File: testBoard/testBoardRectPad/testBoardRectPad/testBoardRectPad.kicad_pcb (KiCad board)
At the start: 2 copper layers, 1 part

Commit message: intermediate commit
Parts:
- removed the REF** at (105.4, 80.0)
- added REF**: DIP-14_W7.62mm, Package_DIP:DIP-14_W7.62mm, F.Cu at (110.1, 70.0)
- added REF**: SOIC-14_3.9x8.7mm_P1.27mm, Package_SO:SOIC-14_3.9x8.7mm_P1.27mm, F.Cu at (0.00, 0.00)
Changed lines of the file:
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@@
     (tracks 0)
     (zones 0)
-    (modules 1)
+    (modules 2)
     (nets 1)
   )
@@
     (mod_text_size 1 1)
     (mod_text_width 0.15)
-    (pad_size 5.3 7)
-    (pad_drill 0.8001)
+    (pad_size 1.95 0.6)
+    (pad_drill 0)
     (pad_to_mask_clearance 0.051)
     (solder_mask_min_width 0.25)
@@
     (visible_elements FFFFFF7F)
     (pcbplotparams
-      (layerselection 0x00000_ffffffff)
+      (layerselection 0x00000_7fffffff)
       (usegerberextensions false)
       (usegerberattributes false)
@@
       (psnegative false)
       (psa4output false)
-      (plotreference true)
-      (plotvalue true)
+      (plotreference false)
+      (plotvalue false)
       (plotinvisibletext false)
       (padsonsilk false)
@@
     (uvia_drill 0.1)
   )
-  (module Connector_Wire:SolderWirePad_1x01_Drill0.8mm (layer F.Cu)
-    (at 105.41 80.01)
-    (descr "Wire solder connection")
-    (tags connector)
-    (attr virtual)
-    (fp_text reference REF** (at 0 -2.54) (layer F.SilkS)
+  (module Package_DIP:DIP-14_W7.62mm (layer F.Cu)
+    (at 110.1 70)
+    (descr "14-lead though-hole mounted DIP package, row spacing 7.62 mm (300 mils)")
+    (tags "THT DIP DIL PDIP 2.54mm 7.62mm 300mil")
+    (fp_text reference REF** (at 3.81 -2.33) (layer F.SilkS)
       (effects (font (size 1 1) (thickness 0.15)))
     )
-    (fp_text value SolderWirePad_1x01_Drill0.8mm (at 0 2.54) (layer F.Fab)
+    (fp_text value DIP-14_W7.62mm (at 3.81 17.57) (layer F.Fab)
       (effects (font (size 1 1) (thickness 0.15)))
     )
-    (fp_line (start 1.5 1.5) (end -1.5 1.5) (layer F.CrtYd) (width 0.05))
-    (fp_line (start 1.5 1.5) (end 1.5 -1.5) (layer F.CrtYd) (width 0.05))
-    (fp_line (start -1.5 -1.5) (end -1.5 1.5) (layer F.CrtYd) (width 0.05))
-    (fp_line (start -1.5 -1.5) (end 1.5 -1.5) (layer F.CrtYd) (width 0.05))
-    (fp_text user %R (at 0 0) (layer F.Fab)
+    (fp_text user %R (at 3.81 7.62) (layer F.Fab)
       (effects (font (size 1 1) (thickness 0.15)))
     )
-    (pad 1 thru_hole rect (at 0 0) (size 5.3 7) (drill 0.8001) (layers *.Cu *.Mask))
+    (fp_line (start 8.7 -1.55) (end -1.1 -1.55) (layer F.CrtYd) (width 0.05))
+    (fp_line (start 8.7 16.8) (end 8.7 -1.55) (layer F.CrtYd) (width 0.05))
+    (fp_line (start -1.1 16.8) (end 8.7 16.8) (layer F.CrtYd) (width 0.05))
+    (fp_line (start -1.1 -1.55) (end -1.1 16.8) (layer F.CrtYd) (width 0.05))
+    (fp_line (start 6.46 -1.33) (end 4.81 -1.33) (layer F.SilkS) (width 0.12))
+    (fp_line (start 6.46 16.57) (end 6.46 -1.33) (layer F.SilkS) (width 0.12))
+    (fp_line (start 1.16 16.57) (end 6.46 16.57) (layer F.SilkS) (width 0.12))
+    (fp_line (start 1.16 -1.33) (end 1.16 16.57) (layer F.SilkS) (width 0.12))
+    (fp_line (start 2.81 -1.33) (end 1.16 -1.33) (layer F.SilkS) (width 0.12))
+    (fp_line (start 0.635 -0.27) (end 1.635 -1.27) (layer F.Fab) (width 0.1))
+    (fp_line (start 0.635 16.51) (end 0.635 -0.27) (layer F.Fab) (width 0.1))
+    (fp_line (start 6.985 16.51) (end 0.635 16.51) (layer F.Fab) (width 0.1))
+    (fp_line (start 6.985 -1.27) (end 6.985 16.51) (layer F.Fab) (width 0.1))
+    (fp_line (start 1.635 -1.27) (end 6.985 -1.27) (layer F.Fab) (width 0.1))
+    (fp_arc (start 3.81 -1.33) (end 2.81 -1.33) (angle -180) (layer F.SilkS) (width 0.12))
+    (pad 14 thru_hole oval (at 7.62 0) (size 1.6 1.6) (drill 0.8) (layers *.Cu *.Mask))
+    (pad 7 thru_hole oval (at 0 15.24) (size 1.6 1.6) (drill 0.8) (layers *.Cu *.Mask))
+    (pad 13 thru_hole oval (at 7.62 2.54) (size 1.6 1.6) (drill 0.8) (layers *.Cu *.Mask))
+    (pad 6 thru_hole oval (at 0 12.7) (size 1.6 1.6) (drill 0.8) (layers *.Cu *.Mask))
+    (pad 12 thru_hole oval (at 7.62 5.08) (size 1.6 1.6) (drill 0.8) (layers *.Cu *.Mask))
+    (pad 5 thru_hole oval (at 0 10.16) (size 1.6 1.6) (drill 0.8) (layers *.Cu *.Mask))
+    (pad 11 thru_hole oval (at 7.62 7.62) (size 1.6 1.6) (drill 0.8) (layers *.Cu *.Mask))
+    (pad 4 thru_hole oval (at 0 7.62) (size 1.6 1.6) (drill 0.8) (layers *.Cu *.Mask))
+    (pad 10 thru_hole oval (at 7.62 10.16) (size 1.6 1.6) (drill 0.8) (layers *.Cu *.Mask))
+    (pad 3 thru_hole oval (at 0 5.08) (size 1.6 1.6) (drill 0.8) (layers *.Cu *.Mask))
+    (pad 9 thru_hole oval (at 7.62 12.7) (size 1.6 1.6) (drill 0.8) (layers *.Cu *.Mask))
+    (pad 2 thru_hole oval (at 0 2.54) (size 1.6 1.6) (drill 0.8) (layers *.Cu *.Mask))
+    (pad 8 thru_hole oval (at 7.62 15.24) (size 1.6 1.6) (drill 0.8) (layers *.Cu *.Mask))
+    (pad 1 thru_hole rect (at 0 0) (size 1.6 1.6) (drill 0.8) (layers *.Cu *.Mask))
+    (model ${KISYS3DMOD}/Package_DIP.3dshapes/DIP-14_W7.62mm.wrl
+      (at (xyz 0 0 0))
+      (scale (xyz 1 1 1))
+      (rotate (xyz 0 0 0))
+    )
+  )
+  (module Package_SO:SOIC-14_3.9x8.7mm_P1.27mm (layer F.Cu)
+    (at 0 0)
+    (descr "SOIC, 14 Pin (JEDEC MS-012AB, https://www.analog.com/media/en/package-pcb-resources/package/pkg_pdf/soic_narrow-r/r_14.pdf), generated with kicad-footprint-generator ipc_gullwing_generator.py")
+    (tags "SOIC SO")
+    (attr smd)
+    (fp_text reference REF** (at 0 -5.28) (layer F.SilkS)
+      (effects (font (size 1 1) (thickness 0.15)))
+    )
+    (fp_text value SOIC-14_3.9x8.7mm_P1.27mm (at 0 5.28) (layer F.Fab)
+      (effects (font (size 1 1) (thickness 0.15)))
+    )
+    (fp_line (start 0 4.435) (end 1.95 4.435) (layer F.SilkS) (width 0.12))
+    (fp_line (start 0 4.435) (end -1.95 4.435) (layer F.SilkS) (width 0.12))
+    (fp_line (start 0 -4.435) (end 1.95 -4.435) (layer F.SilkS) (width 0.12))
+    (fp_line (start 0 -4.435) (end -3.45 -4.435) (layer F.SilkS) (width 0.12))
+    (fp_line (start -0.975 -4.325) (end 1.95 -4.325) (layer F.Fab) (width 0.1))
+    (fp_line (start 1.95 -4.325) (end 1.95 4.325) (layer F.Fab) (width 0.1))
+    (fp_line (start 1.95 4.325) (end -1.95 4.325) (layer F.Fab) (width 0.1))
+    (fp_line (start -1.95 4.325) (end -1.95 -3.35) (layer F.Fab) (width 0.1))
+    (fp_line (start -1.95 -3.35) (end -0.975 -4.325) (layer F.Fab) (width 0.1))
+    (fp_line (start -3.7 -4.58) (end -3.7 4.58) (layer F.CrtYd) (width 0.05))
+    (fp_line (start -3.7 4.58) (end 3.7 4.58) (layer F.CrtYd) (width 0.05))
+    (fp_line (start 3.7 4.58) (end 3.7 -4.58) (layer F.CrtYd) (width 0.05))
+    (fp_line (start 3.7 -4.58) (end -3.7 -4.58) (layer F.CrtYd) (width 0.05))
+    (fp_text user %R (at 0 0) (layer F.Fab)
+      (effects (font (size 0.98 0.98) (thickness 0.15)))
+    )
+    (pad 1 smd roundrect (at -2.475 -3.81) (size 1.95 0.6) (layers F.Cu F.Paste F.Mask) (roundrect_rratio 0.25))
+    (pad 2 smd roundrect (at -2.475 -2.54) (size 1.95 0.6) (layers F.Cu F.Paste F.Mask) (roundrect_rratio 0.25))
+    (pad 3 smd roundrect (at -2.475 -1.27) (size 1.95 0.6) (layers F.Cu F.Paste F.Mask) (roundrect_rratio 0.25))
+    (pad 4 smd roundrect (at -2.475 0) (size 1.95 0.6) (layers F.Cu F.Paste F.Mask) (roundrect_rratio 0.25))
+    (pad 5 smd roundrect (at -2.475 1.27) (size 1.95 0.6) (layers F.Cu F.Paste F.Mask) (roundrect_rratio 0.25))
+    (pad 6 smd roundrect (at -2.475 2.54) (size 1.95 0.6) (layers F.Cu F.Paste F.Mask) (roundrect_rratio 0.25))
+    (pad 7 smd roundrect (at -2.475 3.81) (size 1.95 0.6) (layers F.Cu F.Paste F.Mask) (roundrect_rratio 0.25))
+    (pad 8 smd roundrect (at 2.475 3.81) (size 1.95 0.6) (layers F.Cu F.Paste F.Mask) (roundrect_rratio 0.25))
+    (pad 9 smd roundrect (at 2.475 2.54) (size 1.95 0.6) (layers F.Cu F.Paste F.Mask) (roundrect_rratio 0.25))
+    (pad 10 smd roundrect (at 2.475 1.27) (size 1.95 0.6) (layers F.Cu F.Paste F.Mask) (roundrect_rratio 0.25))
+    (pad 11 smd roundrect (at 2.475 0) (size 1.95 0.6) (layers F.Cu F.Paste F.Mask) (roundrect_rratio 0.25))
+    (pad 12 smd roundrect (at 2.475 -1.27) (size 1.95 0.6) (layers F.Cu F.Paste F.Mask) (roundrect_rratio 0.25))
+    (pad 13 smd roundrect (at 2.475 -2.54) (size 1.95 0.6) (layers F.Cu F.Paste F.Mask) (roundrect_rratio 0.25))
+    (pad 14 smd roundrect (at 2.475 -3.81) (size 1.95 0.6) (layers F.Cu F.Paste F.Mask) (roundrect_rratio 0.25))
+    (pad 15 smd circle (at 8.89 -6.35) (size 1.524 1.524) (layers F.Cu F.Paste F.Mask))
+    (model ${KISYS3DMOD}/Package_SO.3dshapes/SOIC-14_3.9x8.7mm_P1.27mm.wrl
+      (at (xyz 0 0 0))
+      (scale (xyz 1 1 1))
+      (rotate (xyz 0 0 0))
+    )
   )
 )

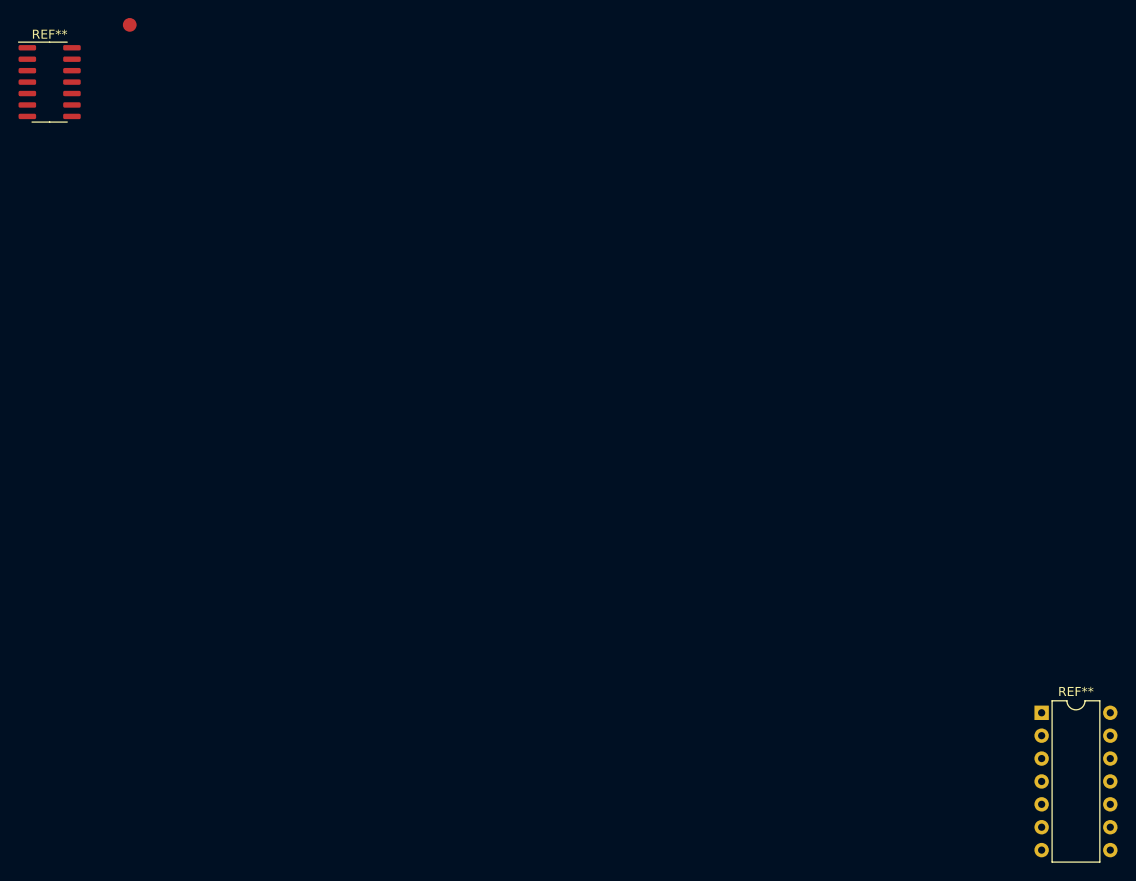
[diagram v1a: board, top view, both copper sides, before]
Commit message: Fix vertical and horisontal rect pads size.
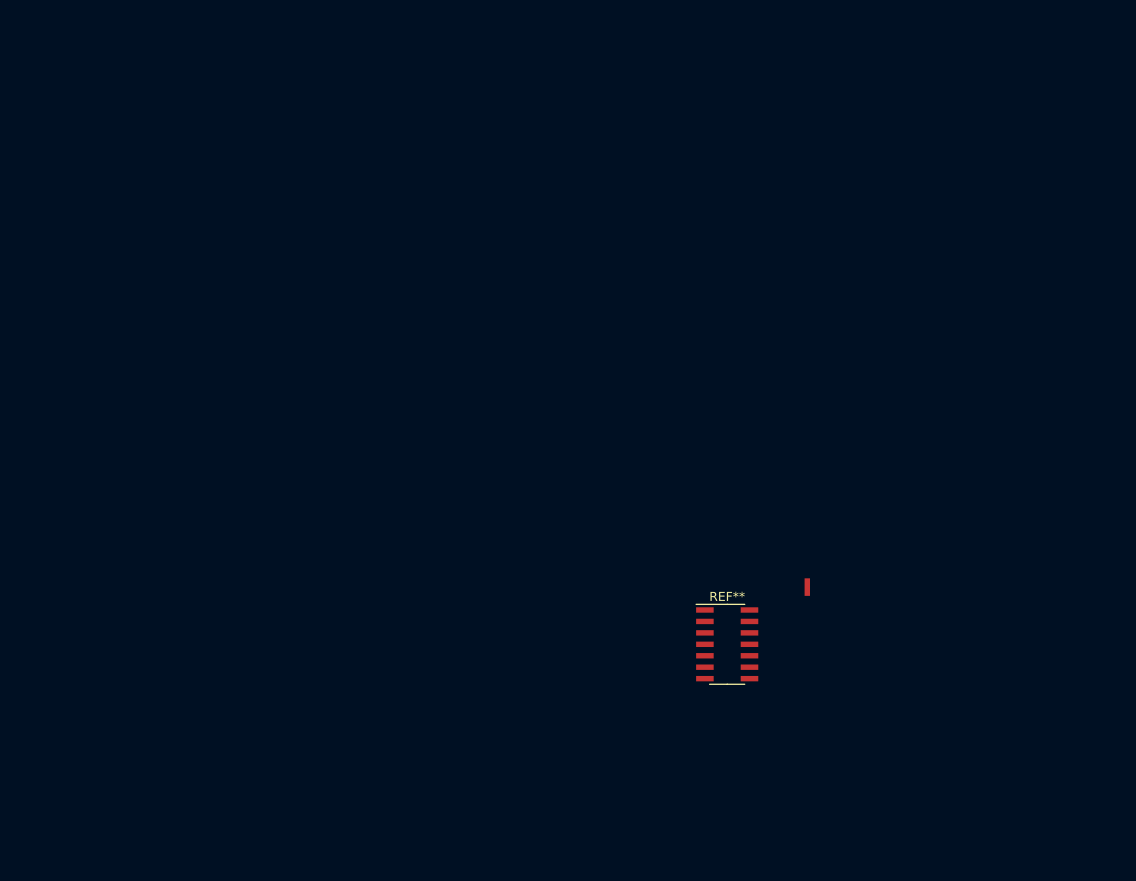
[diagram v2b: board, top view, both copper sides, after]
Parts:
- removed the REF** at (110.1, 70.0)
- moved REF** 97.7 mm to (75.2, 62.4)
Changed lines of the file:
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@@
     (tracks 0)
     (zones 0)
-    (modules 2)
+    (modules 1)
     (nets 1)
   )
@@
     (mod_text_size 1 1)
     (mod_text_width 0.15)
-    (pad_size 1.95 0.6)
+    (pad_size 0.6 1.95)
     (pad_drill 0)
     (pad_to_mask_clearance 0.051)
@@
     (uvia_drill 0.1)
   )
-  (module Package_DIP:DIP-14_W7.62mm (layer F.Cu)
-    (at 110.1 70)
-    (descr "14-lead though-hole mounted DIP package, row spacing 7.62 mm (300 mils)")
-    (tags "THT DIP DIL PDIP 2.54mm 7.62mm 300mil")
-    (fp_text reference REF** (at 3.81 -2.33) (layer F.SilkS)
-      (effects (font (size 1 1) (thickness 0.15)))
-    )
-    (fp_text value DIP-14_W7.62mm (at 3.81 17.57) (layer F.Fab)
-      (effects (font (size 1 1) (thickness 0.15)))
-    )
-    (fp_text user %R (at 3.81 7.62) (layer F.Fab)
-      (effects (font (size 1 1) (thickness 0.15)))
-    )
-    (fp_line (start 8.7 -1.55) (end -1.1 -1.55) (layer F.CrtYd) (width 0.05))
-    (fp_line (start 8.7 16.8) (end 8.7 -1.55) (layer F.CrtYd) (width 0.05))
-    (fp_line (start -1.1 16.8) (end 8.7 16.8) (layer F.CrtYd) (width 0.05))
-    (fp_line (start -1.1 -1.55) (end -1.1 16.8) (layer F.CrtYd) (width 0.05))
-    (fp_line (start 6.46 -1.33) (end 4.81 -1.33) (layer F.SilkS) (width 0.12))
-    (fp_line (start 6.46 16.57) (end 6.46 -1.33) (layer F.SilkS) (width 0.12))
-    (fp_line (start 1.16 16.57) (end 6.46 16.57) (layer F.SilkS) (width 0.12))
-    (fp_line (start 1.16 -1.33) (end 1.16 16.57) (layer F.SilkS) (width 0.12))
-    (fp_line (start 2.81 -1.33) (end 1.16 -1.33) (layer F.SilkS) (width 0.12))
-    (fp_line (start 0.635 -0.27) (end 1.635 -1.27) (layer F.Fab) (width 0.1))
-    (fp_line (start 0.635 16.51) (end 0.635 -0.27) (layer F.Fab) (width 0.1))
-    (fp_line (start 6.985 16.51) (end 0.635 16.51) (layer F.Fab) (width 0.1))
-    (fp_line (start 6.985 -1.27) (end 6.985 16.51) (layer F.Fab) (width 0.1))
-    (fp_line (start 1.635 -1.27) (end 6.985 -1.27) (layer F.Fab) (width 0.1))
-    (fp_arc (start 3.81 -1.33) (end 2.81 -1.33) (angle -180) (layer F.SilkS) (width 0.12))
-    (pad 14 thru_hole oval (at 7.62 0) (size 1.6 1.6) (drill 0.8) (layers *.Cu *.Mask))
-    (pad 7 thru_hole oval (at 0 15.24) (size 1.6 1.6) (drill 0.8) (layers *.Cu *.Mask))
-    (pad 13 thru_hole oval (at 7.62 2.54) (size 1.6 1.6) (drill 0.8) (layers *.Cu *.Mask))
-    (pad 6 thru_hole oval (at 0 12.7) (size 1.6 1.6) (drill 0.8) (layers *.Cu *.Mask))
-    (pad 12 thru_hole oval (at 7.62 5.08) (size 1.6 1.6) (drill 0.8) (layers *.Cu *.Mask))
-    (pad 5 thru_hole oval (at 0 10.16) (size 1.6 1.6) (drill 0.8) (layers *.Cu *.Mask))
-    (pad 11 thru_hole oval (at 7.62 7.62) (size 1.6 1.6) (drill 0.8) (layers *.Cu *.Mask))
-    (pad 4 thru_hole oval (at 0 7.62) (size 1.6 1.6) (drill 0.8) (layers *.Cu *.Mask))
-    (pad 10 thru_hole oval (at 7.62 10.16) (size 1.6 1.6) (drill 0.8) (layers *.Cu *.Mask))
-    (pad 3 thru_hole oval (at 0 5.08) (size 1.6 1.6) (drill 0.8) (layers *.Cu *.Mask))
-    (pad 9 thru_hole oval (at 7.62 12.7) (size 1.6 1.6) (drill 0.8) (layers *.Cu *.Mask))
-    (pad 2 thru_hole oval (at 0 2.54) (size 1.6 1.6) (drill 0.8) (layers *.Cu *.Mask))
-    (pad 8 thru_hole oval (at 7.62 15.24) (size 1.6 1.6) (drill 0.8) (layers *.Cu *.Mask))
-    (pad 1 thru_hole rect (at 0 0) (size 1.6 1.6) (drill 0.8) (layers *.Cu *.Mask))
-    (model ${KISYS3DMOD}/Package_DIP.3dshapes/DIP-14_W7.62mm.wrl
-      (at (xyz 0 0 0))
-      (scale (xyz 1 1 1))
-      (rotate (xyz 0 0 0))
-    )
-  )
   (module Package_SO:SOIC-14_3.9x8.7mm_P1.27mm (layer F.Cu)
-    (at 0 0)
+    (at 75.2 62.4)
     (descr "SOIC, 14 Pin (JEDEC MS-012AB, https://www.analog.com/media/en/package-pcb-resources/package/pkg_pdf/soic_narrow-r/r_14.pdf), generated with kicad-footprint-generator ipc_gullwing_generator.py")
     (tags "SOIC SO")
@@
       (effects (font (size 0.98 0.98) (thickness 0.15)))
     )
-    (pad 1 smd roundrect (at -2.475 -3.81) (size 1.95 0.6) (layers F.Cu F.Paste F.Mask) (roundrect_rratio 0.25))
-    (pad 2 smd roundrect (at -2.475 -2.54) (size 1.95 0.6) (layers F.Cu F.Paste F.Mask) (roundrect_rratio 0.25))
-    (pad 3 smd roundrect (at -2.475 -1.27) (size 1.95 0.6) (layers F.Cu F.Paste F.Mask) (roundrect_rratio 0.25))
-    (pad 4 smd roundrect (at -2.475 0) (size 1.95 0.6) (layers F.Cu F.Paste F.Mask) (roundrect_rratio 0.25))
-    (pad 5 smd roundrect (at -2.475 1.27) (size 1.95 0.6) (layers F.Cu F.Paste F.Mask) (roundrect_rratio 0.25))
-    (pad 6 smd roundrect (at -2.475 2.54) (size 1.95 0.6) (layers F.Cu F.Paste F.Mask) (roundrect_rratio 0.25))
-    (pad 7 smd roundrect (at -2.475 3.81) (size 1.95 0.6) (layers F.Cu F.Paste F.Mask) (roundrect_rratio 0.25))
-    (pad 8 smd roundrect (at 2.475 3.81) (size 1.95 0.6) (layers F.Cu F.Paste F.Mask) (roundrect_rratio 0.25))
-    (pad 9 smd roundrect (at 2.475 2.54) (size 1.95 0.6) (layers F.Cu F.Paste F.Mask) (roundrect_rratio 0.25))
-    (pad 10 smd roundrect (at 2.475 1.27) (size 1.95 0.6) (layers F.Cu F.Paste F.Mask) (roundrect_rratio 0.25))
-    (pad 11 smd roundrect (at 2.475 0) (size 1.95 0.6) (layers F.Cu F.Paste F.Mask) (roundrect_rratio 0.25))
-    (pad 12 smd roundrect (at 2.475 -1.27) (size 1.95 0.6) (layers F.Cu F.Paste F.Mask) (roundrect_rratio 0.25))
-    (pad 13 smd roundrect (at 2.475 -2.54) (size 1.95 0.6) (layers F.Cu F.Paste F.Mask) (roundrect_rratio 0.25))
-    (pad 14 smd roundrect (at 2.475 -3.81) (size 1.95 0.6) (layers F.Cu F.Paste F.Mask) (roundrect_rratio 0.25))
-    (pad 15 smd circle (at 8.89 -6.35) (size 1.524 1.524) (layers F.Cu F.Paste F.Mask))
+    (pad 1 smd rect (at -2.475 -3.81) (size 1.95 0.6) (layers F.Cu F.Paste F.Mask))
+    (pad 2 smd rect (at -2.475 -2.54) (size 1.95 0.6) (layers F.Cu F.Paste F.Mask))
+    (pad 3 smd rect (at -2.475 -1.27) (size 1.95 0.6) (layers F.Cu F.Paste F.Mask))
+    (pad 4 smd rect (at -2.475 0) (size 1.95 0.6) (layers F.Cu F.Paste F.Mask))
+    (pad 5 smd rect (at -2.475 1.27) (size 1.95 0.6) (layers F.Cu F.Paste F.Mask))
+    (pad 6 smd rect (at -2.475 2.54) (size 1.95 0.6) (layers F.Cu F.Paste F.Mask))
+    (pad 7 smd rect (at -2.475 3.81) (size 1.95 0.6) (layers F.Cu F.Paste F.Mask))
+    (pad 8 smd rect (at 2.475 3.81) (size 1.95 0.6) (layers F.Cu F.Paste F.Mask))
+    (pad 9 smd rect (at 2.475 2.54) (size 1.95 0.6) (layers F.Cu F.Paste F.Mask))
+    (pad 10 smd rect (at 2.475 1.27) (size 1.95 0.6) (layers F.Cu F.Paste F.Mask))
+    (pad 11 smd rect (at 2.475 0) (size 1.95 0.6) (layers F.Cu F.Paste F.Mask))
+    (pad 12 smd rect (at 2.475 -1.27) (size 1.95 0.6) (layers F.Cu F.Paste F.Mask))
+    (pad 13 smd rect (at 2.475 -2.54) (size 1.95 0.6) (layers F.Cu F.Paste F.Mask))
+    (pad 14 smd rect (at 2.475 -3.81) (size 1.95 0.6) (layers F.Cu F.Paste F.Mask))
+    (pad 15 smd rect (at 8.89 -6.35) (size 0.6 1.95) (layers F.Cu F.Paste F.Mask))
     (model ${KISYS3DMOD}/Package_SO.3dshapes/SOIC-14_3.9x8.7mm_P1.27mm.wrl
       (at (xyz 0 0 0))
